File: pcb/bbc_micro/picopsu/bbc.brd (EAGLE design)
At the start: 52 x 33 mm, 24 parts, among them U1 TPS60400DVBR, U2 USBC_16P, U3 TPS60400DVBR

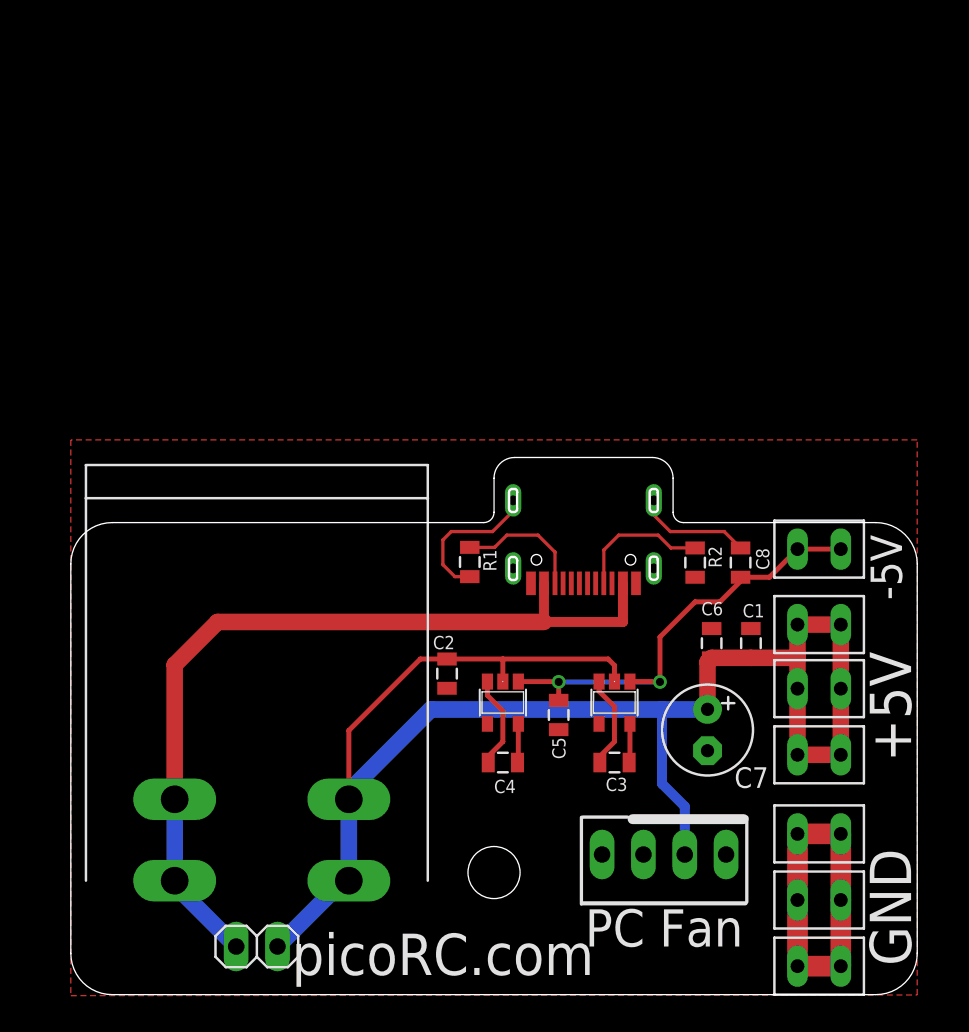
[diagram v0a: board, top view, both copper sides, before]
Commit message: BBC micro USB adaptor
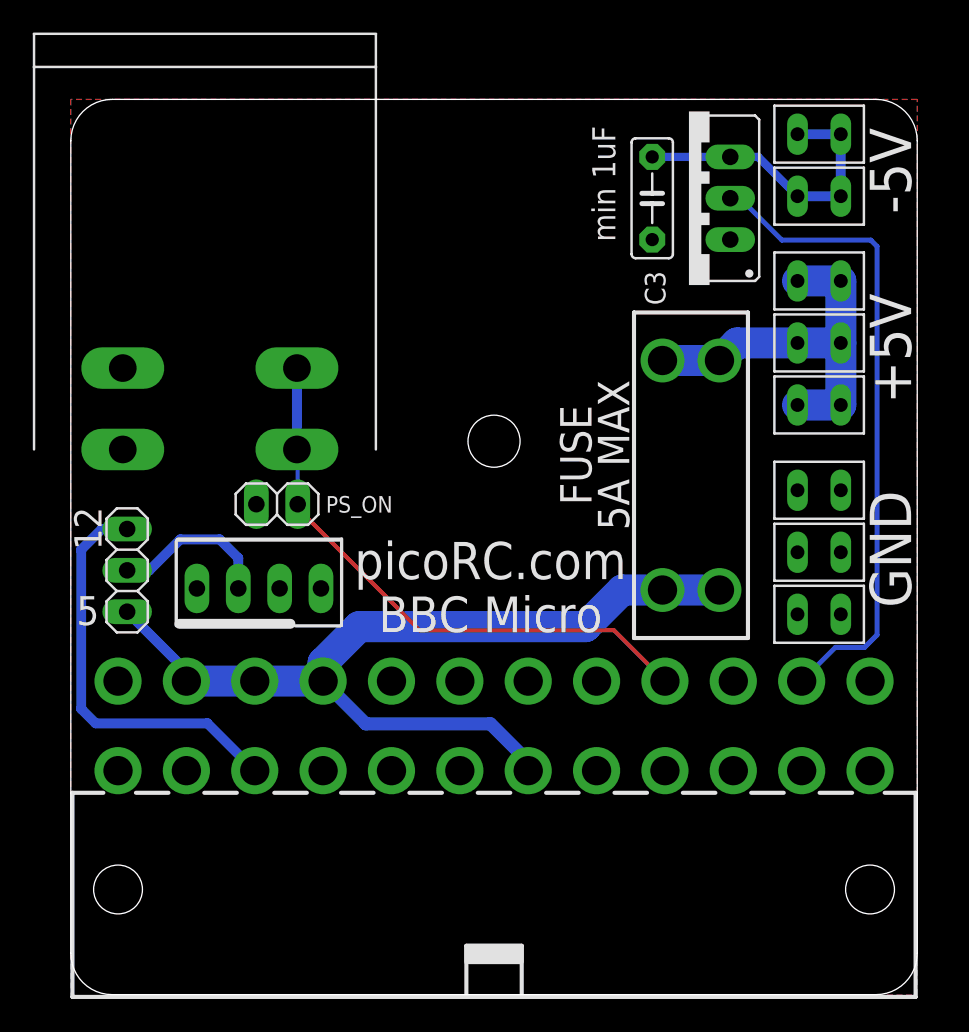
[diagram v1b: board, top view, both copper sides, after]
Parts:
- removed C1, C8: 100nF, clock:0805@1
- removed C2, C4, C6: 1uF, clock:0805@1
- removed C5: 2.2uF, clock:0805@1
- removed C7: (no value), adafruit:E2,5-6
- removed R1, R2: 5K1, atx_power_control:0805
- removed U1, U3: TPS60400DVBR, TPS6040x:SOT23-5
- removed U2: USBC_16P, my_usbc_16p:USBC_16P_FOOT
- added IC1: (no value), v-reg:79XXS
- added J1: ATX24RH, macse:ATX24_RIGHT_ANGLE
- added JP2: (no value), pinhead:1X03
- added U$1: CAR_FUSE_HOLDER3IN1, atx_power_control:FUSE_HOLDER_3IN1
- added U$2: BLADE28, blade:2.8BLADE
- C3: value 1uF -> (none); device clock:0805@1 -> capacitor-wima:C5B2.5
- moved C3 34.7 mm to (35.7, 48.9), turned to 270 degrees
- moved JP3 29.8 mm to (11.6, 25.0), turned to 0 degrees
- moved JP1 27.2 mm to (12.7, 30.1)
- moved U$3 26.7 mm to (8.24, 33.5)
- moved U$4 26.5 mm to (26.0, 34.0)
- moved U$5 25.5 mm to (46.0, 52.9)
- moved U$11 21.6 mm to (46.0, 23.4)
- moved U$8 21.5 mm to (46.0, 36.2)
- moved U$10 21.4 mm to (46.0, 27.2)
- moved U$7 21.2 mm to (46.0, 40.0)
- moved U$6 21.1 mm to (46.0, 43.8)
- moved U$9 21.1 mm to (46.0, 31.0)
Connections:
- removed net -5V: C5.1, C8.2, U$5.P$1, U$5.P$2, U1.1, U3.1
- removed net N$3: C3.1, U3.5
- removed net N$31: R1.1, U2.B5
- removed net N$33: R2.1, U2.A5
- removed net N$4: C4.2, U1.3
- new net +12V: J1.10, JP2.3
- new net -12V: IC1.IN, J1.14
- new net N$6: J1.21, J1.22, J1.23, J1.6, JP2.1, U$1.B0, U$1.B1
- net +5V: now also U$1.A0, U$1.A1; no longer C1.2, C2.2, C6.2, C7.+, JP1.1, JP3.2, U$3.P$2, U$3.P$4, U1.2, U3.2
- net GND: now also C3.2, IC1.GND, J1.15, J1.17, J1.18, J1.19, J1.24, J1.3, J1.5, J1.7, JP1.2, U$3.P$1, U$3.P$3; no longer C1.1, C2.1, C5.2, C6.1, C7.-, C8.1, R1.2, R2.2, U1.4, U2.A1B12, U2.B11A12, U2.P$13, U2.P$14, U2.P$15, U2.P$16, U3.4
- net N$1: now also JP2.2, JP3.2; no longer JP1.2, U$3.P$1, U$3.P$3, U2.A4B9, U2.B4A9
- net N$2: now also C3.1, IC1.OUT, U$2.P$1, U$2.P$2, U$5.P$1, U$5.P$2; no longer C3.2, U3.3
- net N$5: now also J1.16, JP1.1, U$3.P$2, U$3.P$4; no longer C4.1, U1.5
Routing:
- net +5V: track 100.4 -> 24.3 mm
- net N$6: track 0.00 -> 56.7 mm
- net N$1: track 52.3 -> 9.96 mm
- net -12V: track 0.00 -> 39.9 mm
- net GND: track 37.8 -> 0.00 mm
- net N$5: track 2.40 -> 35.6 mm
- net -5V: track 27.9 -> 0.00 mm, vias 2 -> 0
- net +12V: track 0.00 -> 25.4 mm
- net N$2: track 5.74 -> 19.1 mm
- net N$33: track 8.36 -> 0.00 mm
- net N$31: track 7.89 -> 0.00 mm
- net N$4: track 5.74 -> 0.00 mm
- net N$3: track 2.40 -> 0.00 mm
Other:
- board size 52 x 33 mm -> 52 x 55 mm
- board text added: "12"
- board text added: "5"
- board text added: "BBC Micro"
- board text added: "BBC Micro PicoPSU Adaptor"
- board text added: "FUSE 5A MAX"
- board text added: "PS_ON"
- board text added: "PT1 dekuNukem MAR 2023"
- board text added: "min 1uF"
- board text removed: "BBC Micro USB Power Adaptor"
- board text removed: "PC Fan"
- board text removed: "PT2 dekuNukem MAR 2023"
